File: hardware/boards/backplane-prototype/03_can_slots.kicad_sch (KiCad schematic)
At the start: 17 parts, among them J1 SLOT_1, J2 EXTERNAL CAN (GND / CANL / CA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, J3 SLOT_2, J4 SLOT_3, J6 SLOT_4, J7 SLOT_5, J8 SLOT_6, U5 TCAN3413DR

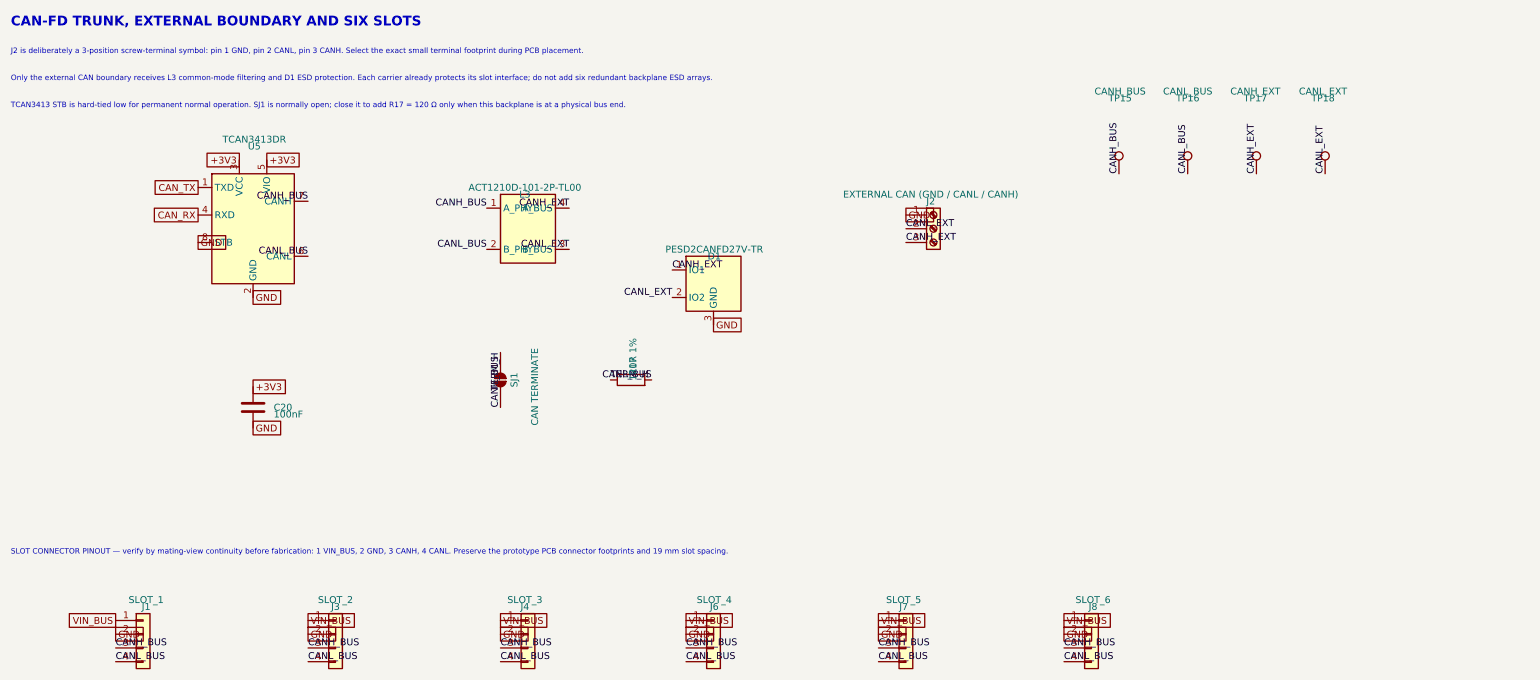
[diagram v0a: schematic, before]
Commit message: checkpoint backplane PCB synchronization
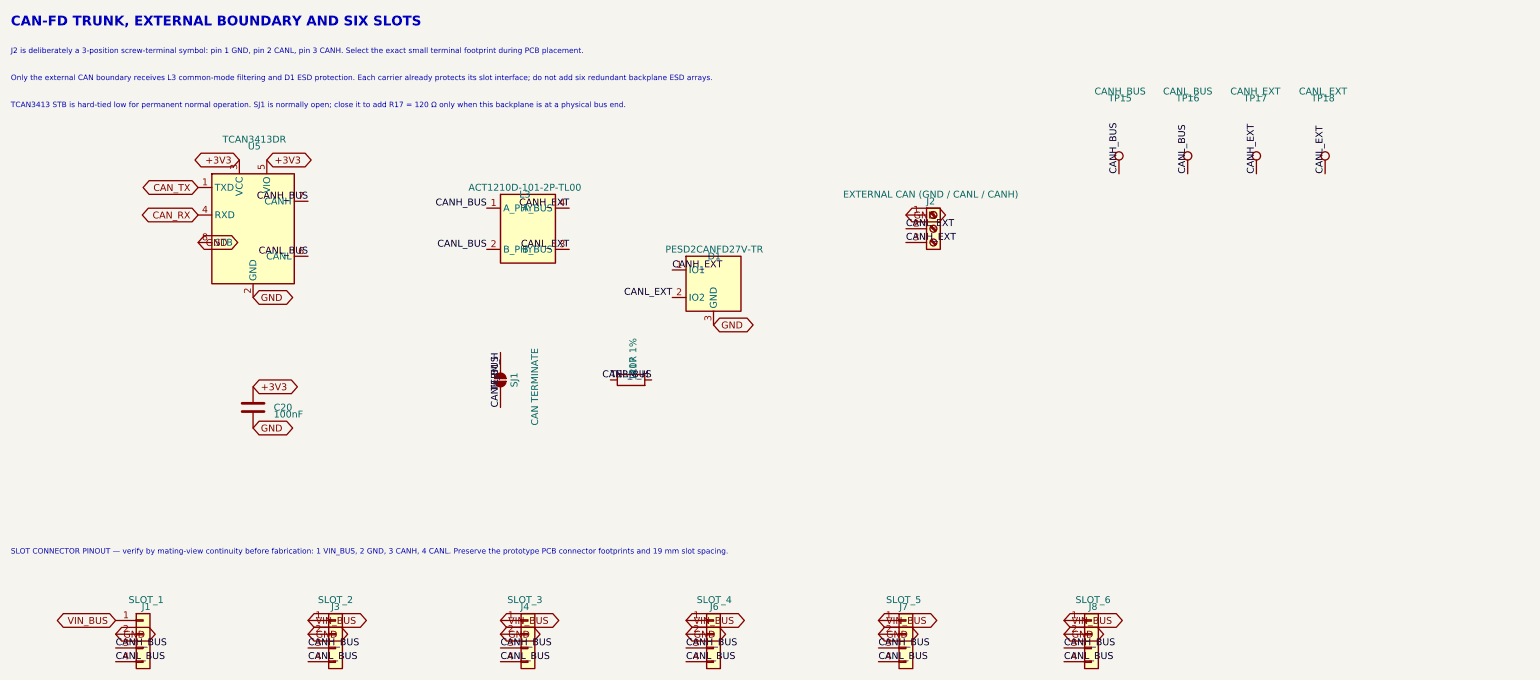
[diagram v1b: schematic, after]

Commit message: hardware: add manual CAN terminal and fix XT30 pinout
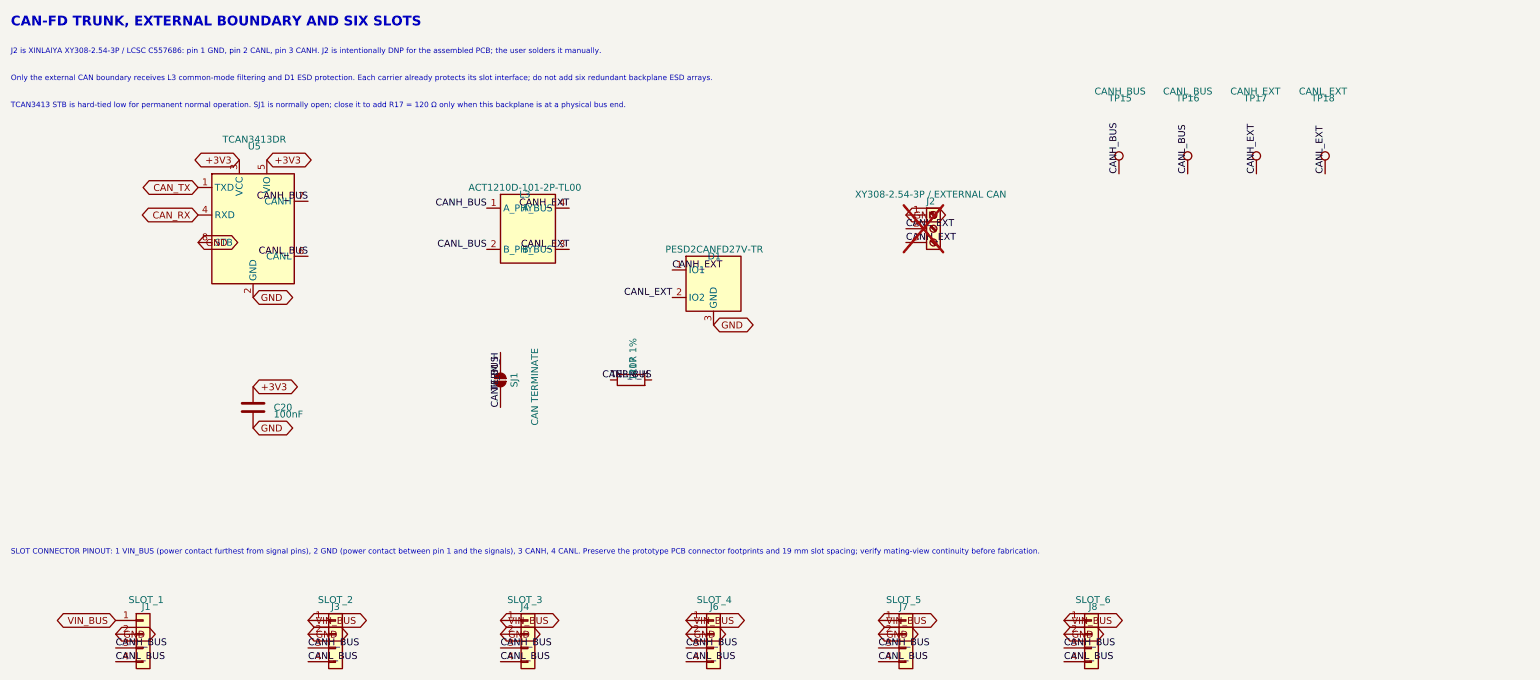
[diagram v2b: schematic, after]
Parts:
- J2: value EXTERNAL CAN (GND / CANL / CANH) -> XY308-2.54-3P / EXTERNAL CAN; footprint (none) -> mini-rack-power:TerminalBlock_Xinya_XY308-2.54-3P_1x03_P2.54mm_Horizontal; LCSC (none) -> C557686; MPN TBD — small 3-position screw terminal -> XY308-2.54-3P; Manufacturer TBD -> XINLAIYA; Package TBD during PCB placement -> THT, 3-position, P2.54 mm, side entry; Population POP after terminal selection -> DNP — user-installed; now not fitted
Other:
- note added: "J2 is XINLAIYA XY308-2.54-3P / LCSC C557686: pin 1 GND, pin 2 CANL, pin 3 CANH. J2 is intentionally DNP for the assembled PCB; the user solders it manually."
- note added: "SLOT CONNECTOR PINOUT: 1 VIN_BUS (power contact furthest from signal pins), 2 GND (power contact between pin 1 and the signals), 3 CANH, 4 CANL. Preserve the prototype PCB connector footprints and 19 mm slot spacing; verify mating-view continuity before fabrication."
- note removed: "J2 is deliberately a 3-position screw-terminal symbol: pin 1 GND, pin 2 CANL, pin 3 CANH. Select the exact small terminal footprint during PCB placement."
- note removed: "SLOT CONNECTOR PINOUT — verify by mating-view continuity before fabrication: 1 VIN_BUS, 2 GND, 3 CANH, 4 CANL. Preserve the prototype PCB connector footprints and 19 mm slot spacing."
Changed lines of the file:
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@@
 	(generator_version "10.0")
 	(paper "A4")
-	(text "SLOT CONNECTOR PINOUT — verify by mating-view continuity before fabrication: 1 VIN_BUS, 2 GND, 3 CANH, 4 CANL. Preserve the prototype PCB connector footprints and 19 mm slot spacing."
+	(text "SLOT CONNECTOR PINOUT: 1 VIN_BUS (power contact furthest from signal pins), 2 GND (power contact between pin 1 and the signals), 3 CANH, 4 CANL. Preserve the prototype PCB connector footprints and 19 mm slot spacing; verify mating-view continuity before fabrication."
 		(exclude_from_sim no)
 		(at 20 115 0)
@@
 		)
 	)
-	(text "J2 is deliberately a 3-position screw-terminal symbol: pin 1 GND, pin 2 CANL, pin 3 CANH. Select the exact small terminal footprint during PCB placement."
+	(text "J2 is XINLAIYA XY308-2.54-3P / LCSC C557686: pin 1 GND, pin 2 CANL, pin 3 CANH. J2 is intentionally DNP for the assembled PCB; the user solders it manually."
 		(exclude_from_sim no)
 		(at 20 22.5 0)
@@
 		(on_board yes)
 		(in_pos_files yes)
-		(dnp no)
+		(dnp yes)
 		(property "Reference" "J2"
 			(at 190 49.53 0)
@@
 			)
 		)
-		(property "Value" "EXTERNAL CAN (GND / CANL / CANH)"
+		(property "Value" "XY308-2.54-3P / EXTERNAL CAN"
 			(at 190 48.26 0)
 			(show_name no)
@@
 			)
 		)
-		(property "Footprint" ""
+		(property "Footprint" "mini-rack-power:TerminalBlock_Xinya_XY308-2.54-3P_1x03_P2.54mm_Horizontal"
 			(at 190 55 0)
 			(hide yes)
@@
 			)
 		)
-		(property "Datasheet" ""
+		(property "Datasheet" "../../../docs/data-sheets/XINLAIYA/XY308-2.54.pdf"
 			(at 190 55 0)
 			(hide yes)
@@
 			)
 		)
-		(property "Description" "Generic screw terminal, single row, 01x03, script generated (kicad-library-utils/schlib/autogen/connector/)"
+		(property "Description" "XINLAIYA XY308-2.54-3P, 3-position 2.54 mm side-entry screw terminal, 6 A 150 V"
 			(at 190 55 0)
 			(hide yes)
@@
 			)
 		)
-		(property "MPN" "TBD — small 3-position screw terminal"
+		(property "MPN" "XY308-2.54-3P"
 			(at 190 55 0)
 			(hide yes)
@@
 			)
 		)
-		(property "Manufacturer" "TBD"
+		(property "Manufacturer" "XINLAIYA"
 			(at 190 55 0)
 			(hide yes)
@@
 			)
 		)
-		(property "LCSC" ""
+		(property "LCSC" "C557686"
 			(at 190 55 0)
 			(hide yes)
@@
 			)
 		)
-		(property "Package" "TBD during PCB placement"
+		(property "Package" "THT, 3-position, P2.54 mm, side entry"
 			(at 190 55 0)
 			(hide yes)
@@
 			)
 		)
-		(property "Population" "POP after terminal selection"
+		(property "Population" "DNP — user-installed"
 			(at 190 55 0)
 			(hide yes)

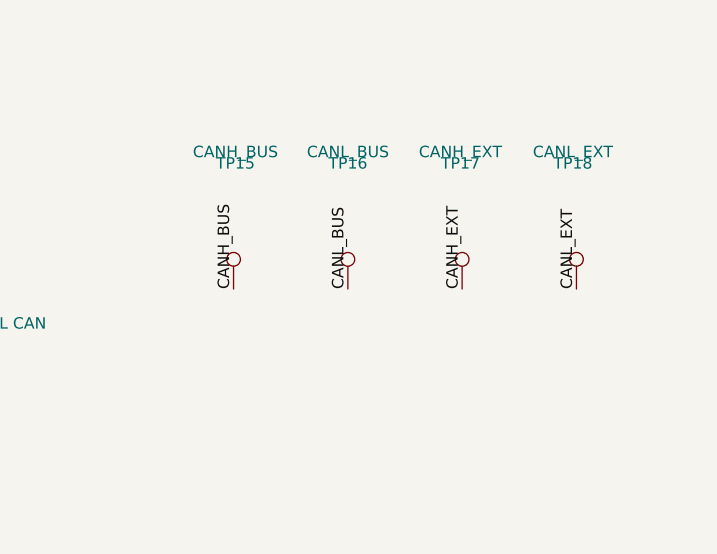
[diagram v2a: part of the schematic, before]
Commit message: hardware: mark all test points DNP
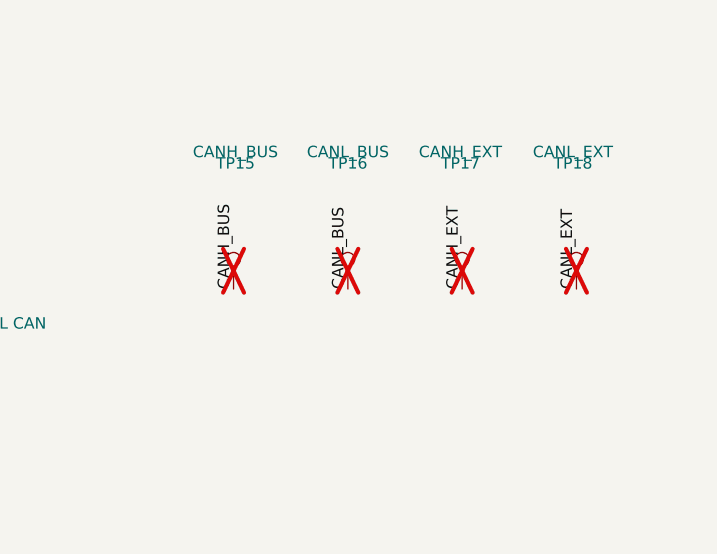
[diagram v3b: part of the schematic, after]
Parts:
- TP15, TP16, TP17, TP18: now not fitted; now left out of the parts list
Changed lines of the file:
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@@
 		(body_style 1)
 		(exclude_from_sim no)
-		(in_bom yes)
+		(in_bom no)
 		(on_board yes)
 		(in_pos_files yes)
-		(dnp no)
+		(dnp yes)
 		(property "Reference" "TP16"
 			(at 237.5 30.48 0)
@@
 		(body_style 1)
 		(exclude_from_sim no)
-		(in_bom yes)
+		(in_bom no)
 		(on_board yes)
 		(in_pos_files yes)
-		(dnp no)
+		(dnp yes)
 		(property "Reference" "TP18"
 			(at 262.5 30.48 0)
@@
 		(body_style 1)
 		(exclude_from_sim no)
-		(in_bom yes)
+		(in_bom no)
 		(on_board yes)
 		(in_pos_files yes)
-		(dnp no)
+		(dnp yes)
 		(property "Reference" "TP17"
 			(at 250 30.48 0)
@@
 		(body_style 1)
 		(exclude_from_sim no)
-		(in_bom yes)
+		(in_bom no)
 		(on_board yes)
 		(in_pos_files yes)
-		(dnp no)
+		(dnp yes)
 		(property "Reference" "TP15"
 			(at 225 30.48 0)
